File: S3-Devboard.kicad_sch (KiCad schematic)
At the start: 16 parts, among them SW1 IO0, SW2 RST, U1 ESP32-S3(R8), U2 W25Q128JVSIQTR, U3 AMS1117-3_3, U4 AMS1117, X1 40MHz

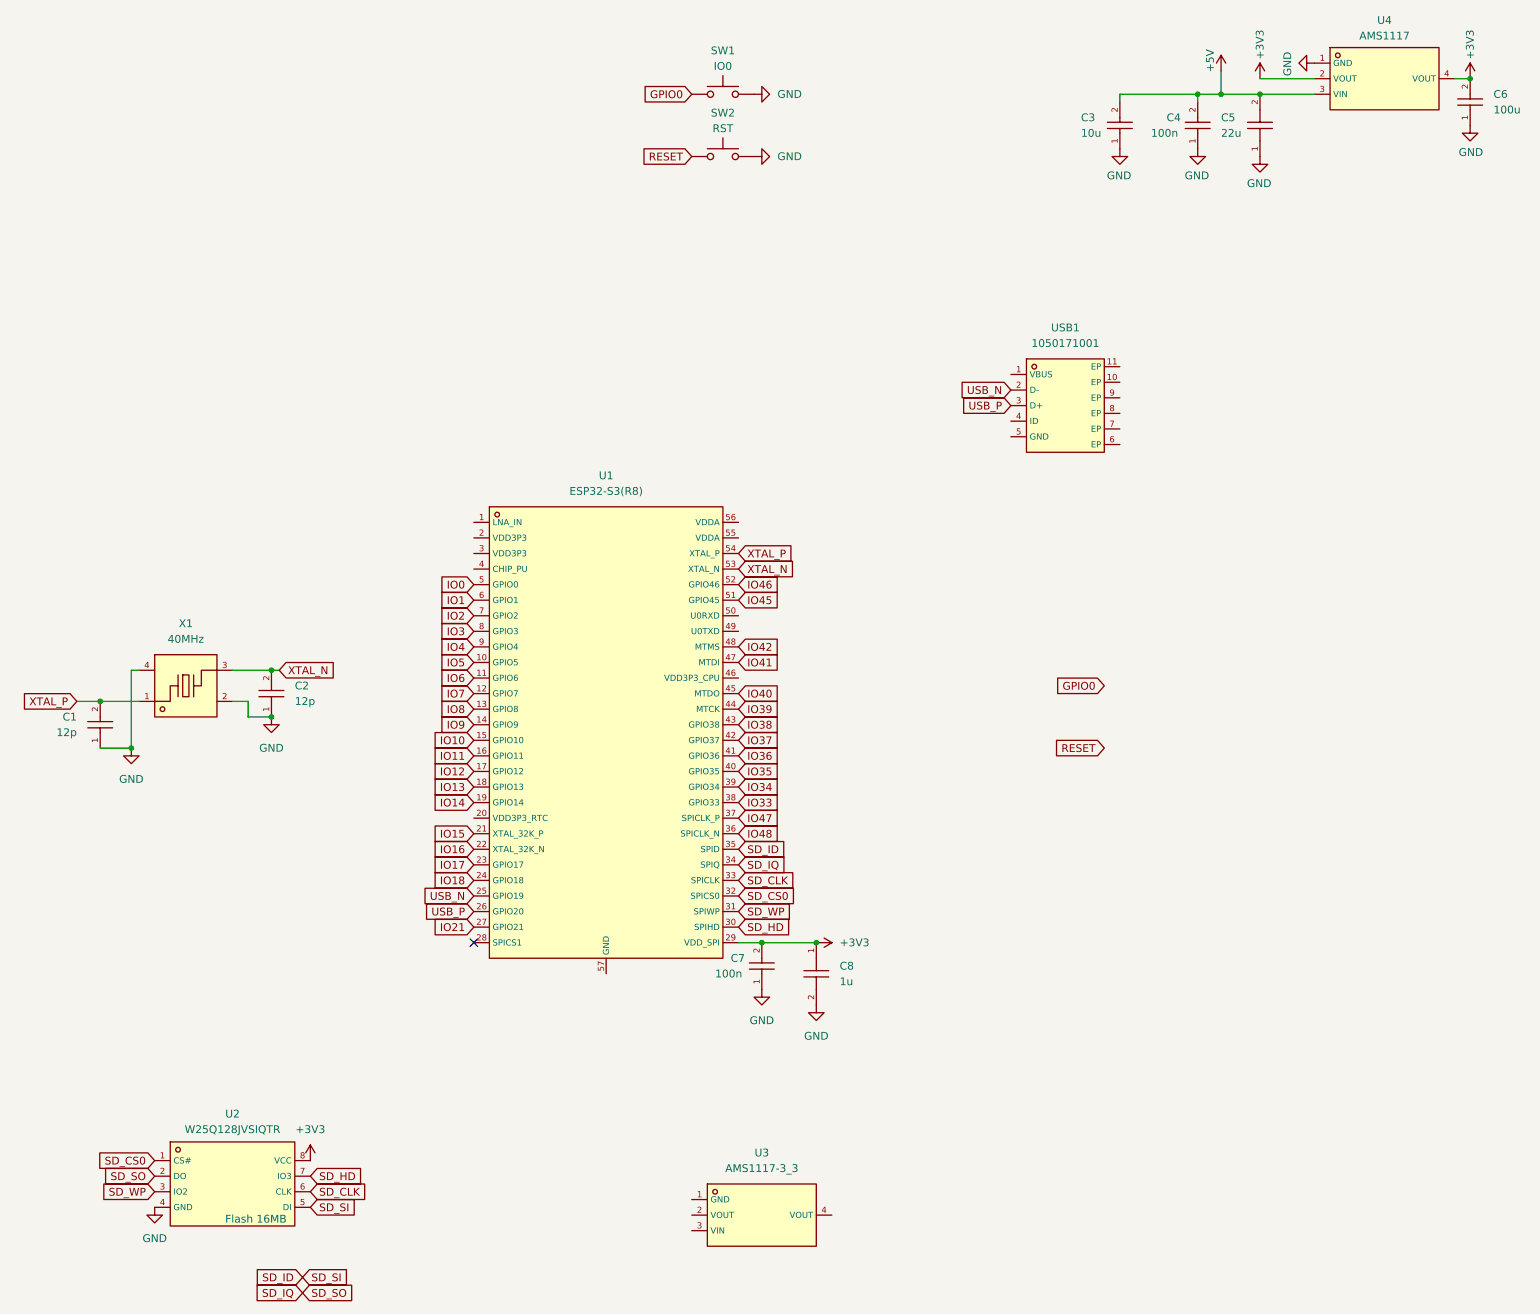
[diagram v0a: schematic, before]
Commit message: Changes
- Add caps for SPI Flash
- Add reset circuit
- Add net classes
- Add VSPI rather than constant 3V3
- Add Schottky diode for the power delivery
- Add PCB Antenna
- Add provisional headers
- Break out the GPIOs to Vias
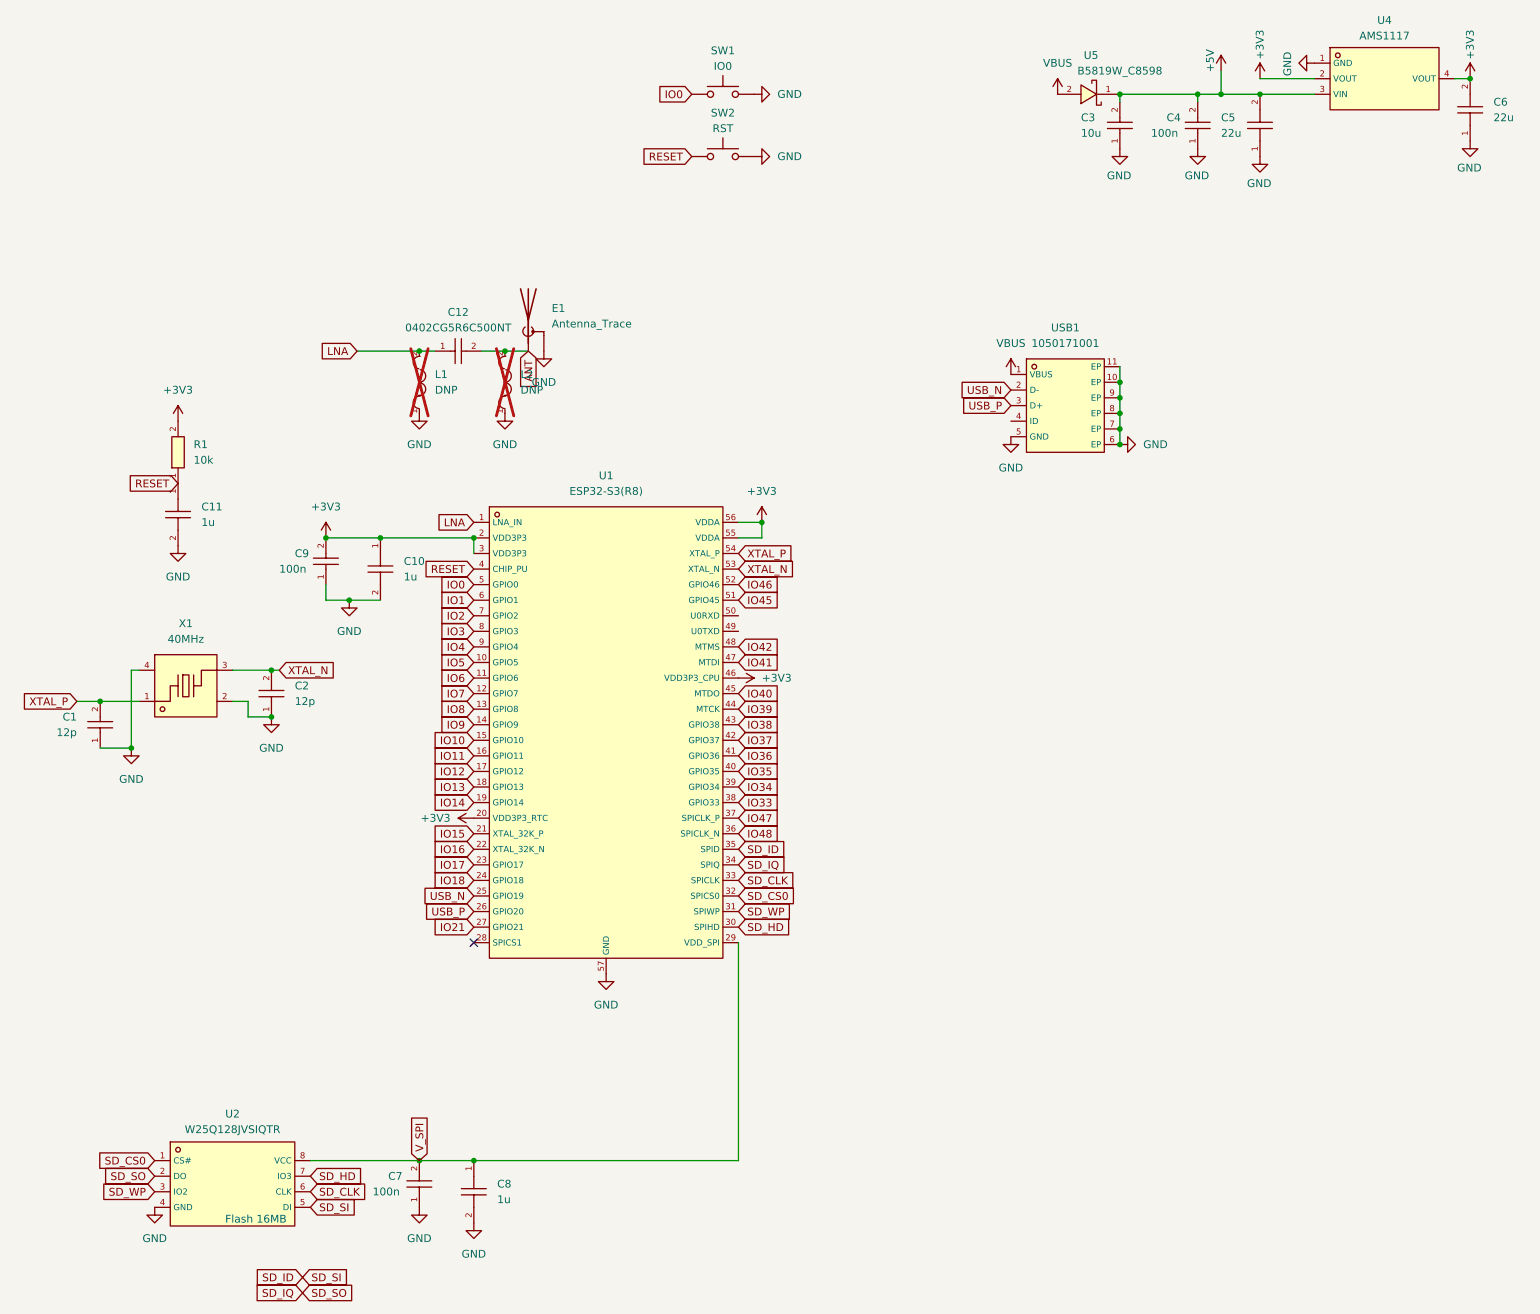
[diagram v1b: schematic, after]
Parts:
- removed C6: 100u, jlc_footprints:C1206, symbol CL31A107MQHNNNE:CL31A107MQHNNNE
- removed U3: AMS1117-3_3, jlc_footprints:SOT-223-3_L6.5-W3.4-P2.30-LS7.0-BR, symbol jlc_symbols:AMS1117-3_3
- added C10, C11: 1u, jlc_footprints:C0402, symbol jlc_symbols:CL05A105KA5NQNC
- added C12: 0402CG5R6C500NT, jlc_footprints:C0402, symbol jlc_symbols:0402CG5R6C500NT
- added C6: 22u, jlc_footprints:C0603, symbol CL10A226MQ8NRNC:CL10A226MQ8NRNC
- added C9: 100n, jlc_footprints:C0402, symbol CL05B104KO5NNNC:CL05B104KO5NNNC
- added E1: Antenna_Trace, RF_Antenna:Texas_SWRA117D_2.4GHz_Right, symbol Device:Antenna_Shield
- added L1, L2: DNP, jlc_footprints:L0603, symbol jlc_symbols:SDFL1608S100KTF
- added R1: 10k, jlc_footprints:R0402, symbol jlc_symbols:0402WGF1002TCE
- added U5: B5819W_C8598, jlc_footprints:SOD-123_L2.7-W1.6-LS3.7-RD-1, symbol jlc_symbols:B5819W_C8598
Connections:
- net GPIO0 is gone; now on net IO0: SW1.2
- net +3V3: now also U1.2 (VDD3P3), U1.20 (VDD3P3_RTC), U1.3 (VDD3P3), U1.46 (VDD3P3_CPU), U1.55 (VDDA), U1.56 (VDDA), C10.1, C6.2, C9.2, R1.2; no longer C7.2, C8.1, U1.29 (VDD_SPI), U2.8 (VCC)
- net +5V: now also U5.1 (-)
- net GND: now also U1.57 (GND), USB1.10 (EP), USB1.11 (EP), USB1.5 (GND), USB1.6 (EP), USB1.7 (EP), USB1.8 (EP), USB1.9 (EP), C10.2, C11.2, C6.1, C9.1, E1.2 (Shield), L1.1, L2.1
- net RESET: now also U1.4 (CHIP_PU), C11.1, R1.1
- net LNA: now reaches U1.1 (LNA_IN)
- net LNA: now also C12.1, L1.2
- net VBUS: now reaches USB1.1 (VBUS)
- net VBUS: now also U5.2 (+)
- new net ANT: C12.2, E1.1 (A), L2.2
- new net V_SPI: C7.2, C8.1, U1.29 (VDD_SPI), U2.8 (VCC)
